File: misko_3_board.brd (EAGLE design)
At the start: 74 x 152 mm, 179 parts, among them IC1 ATMEGA1281-16AU, IC10 ORG1510-MK4, IC11 TPS3808G33DBVT, IC12 LTC4425, IC13 RN-42, IC14 ADXL345, IC15 74HCT1G32, IC16 FM25W256-SOIC, IC17 MICROSD_SPI_MODE, IC18 FH12-30S-0.5SH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

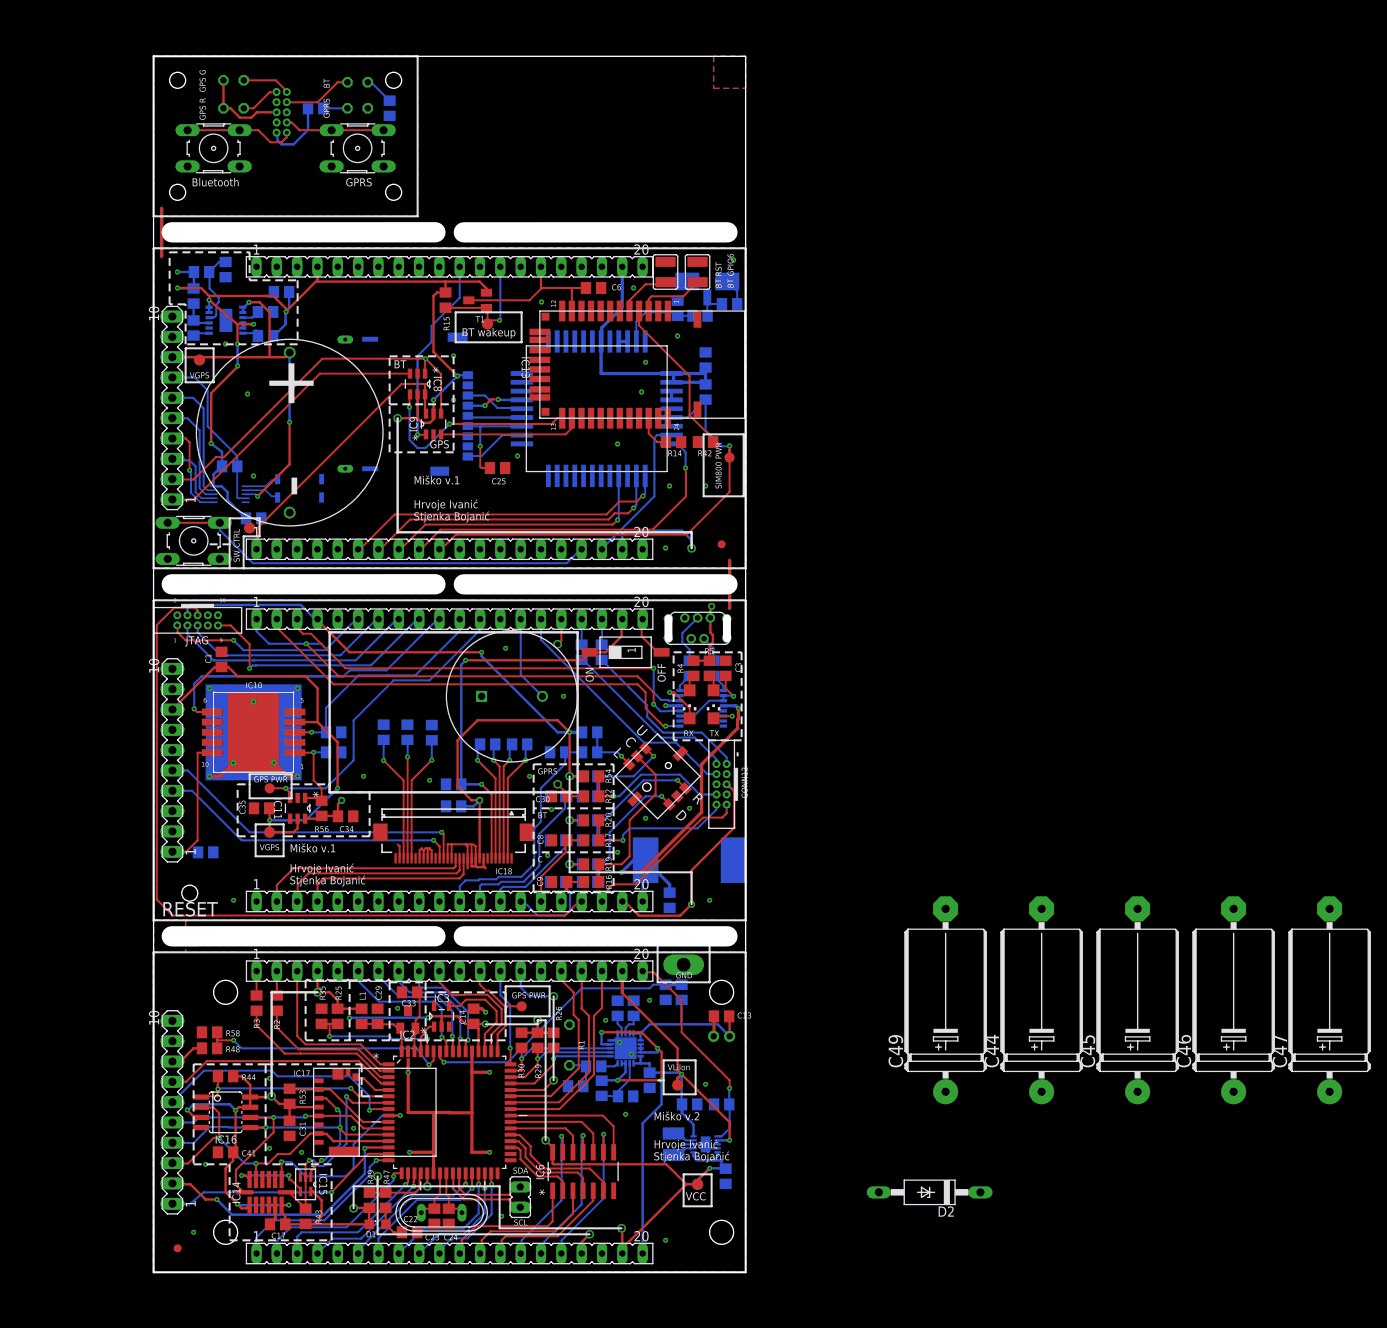
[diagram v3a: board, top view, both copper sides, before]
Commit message: - replaced LTC4425's Vmid capacitor divider by resistors -
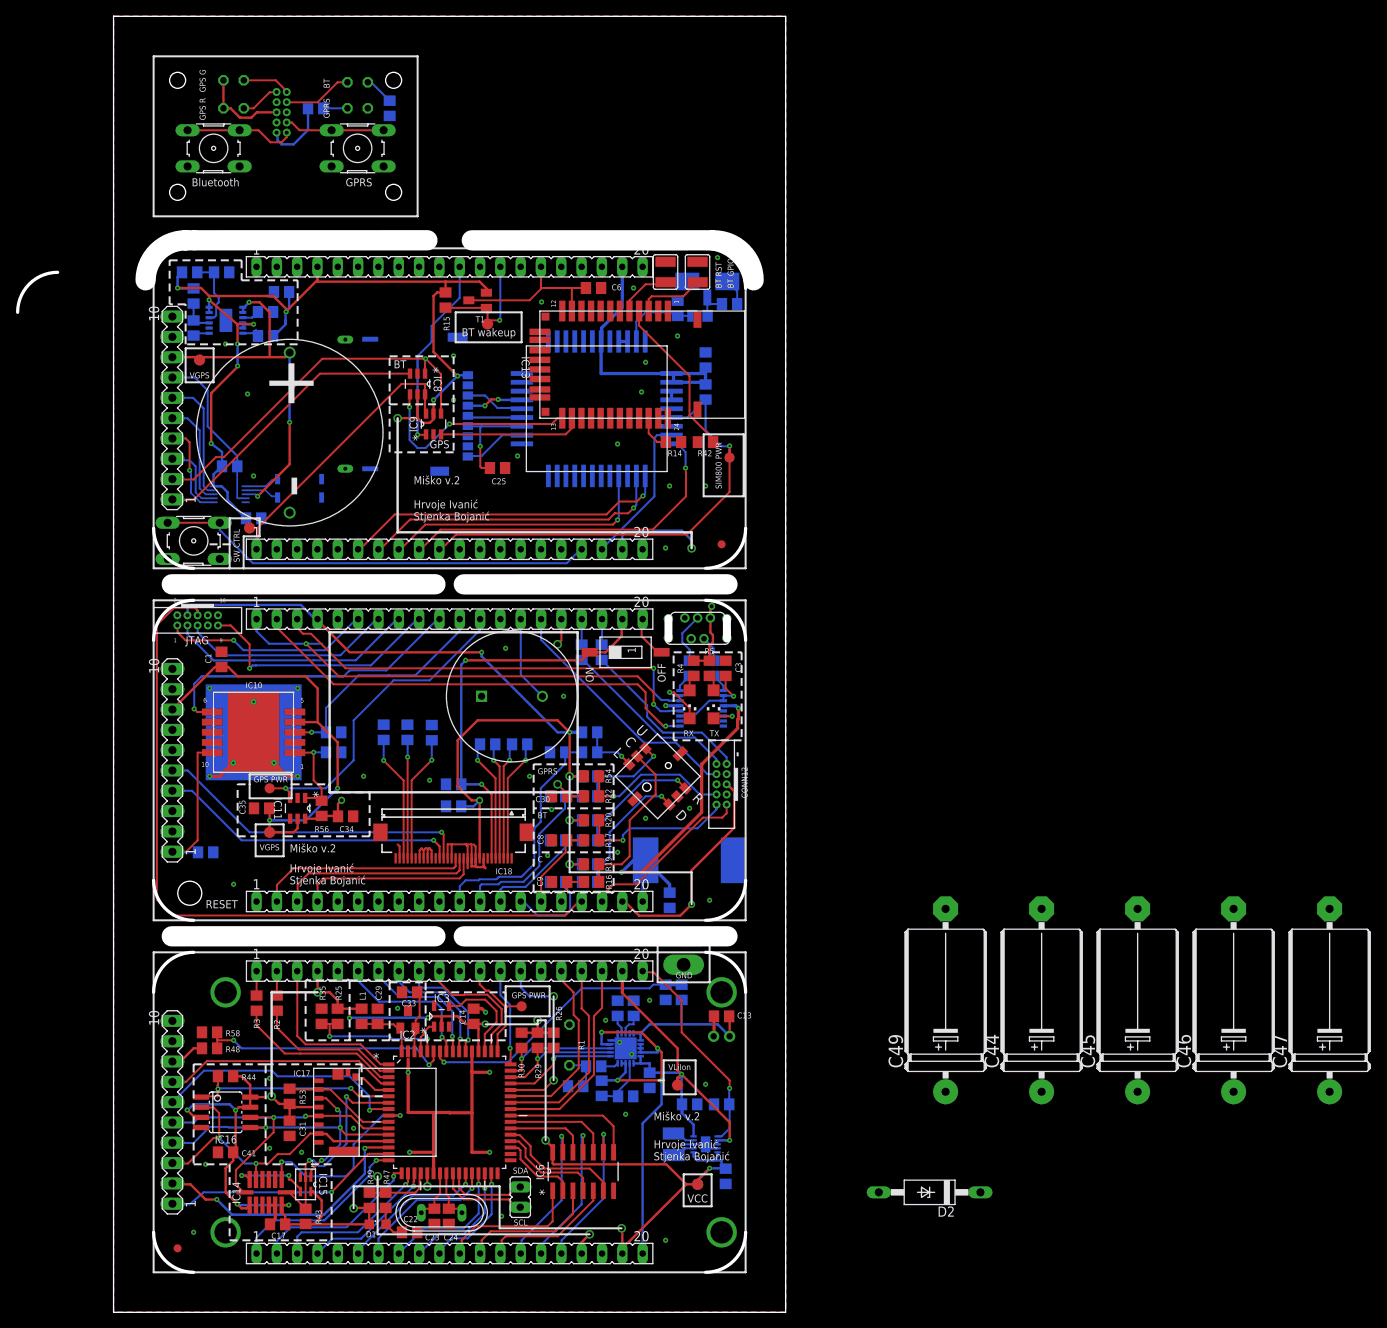
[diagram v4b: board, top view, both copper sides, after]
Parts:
- removed C19, C20: 100µF, rcl:C0805
- added R60, R61: 470k, resistor:R0805
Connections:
- net GND: now also R61.1; no longer C20.1
- net VCC: now also R60.2; no longer C19.1
- net VMID: now also R60.1, R61.2; no longer C19.2, C20.2
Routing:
- net GND: track 121.8 -> 97.8 mm, vias 53 -> 57
- net VCC: track 462.2 -> 459.8 mm, vias 35 -> 34
- net VMID: track 9.76 -> 9.00 mm
- removed copper zone on layer 1, net N$1
- removed copper zone on layer 16, net N$2
- removed copper zone on layer 16, net N$3
- removed copper zone on layer 1, net N$4
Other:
- board size 74 x 152 mm -> 96 x 162 mm
- board text removed: "Miško v.1"

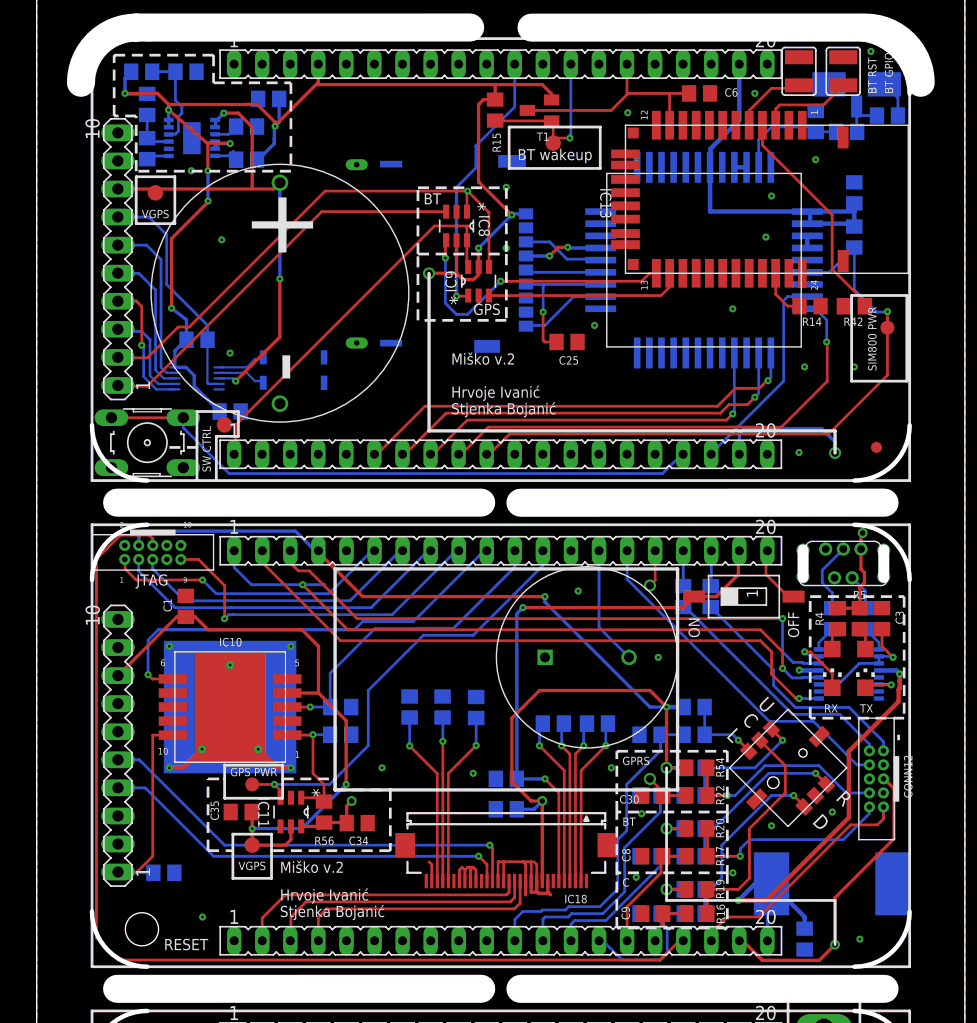
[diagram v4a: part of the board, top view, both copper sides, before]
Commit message: - replaced TH reset switch with smaller SMD part
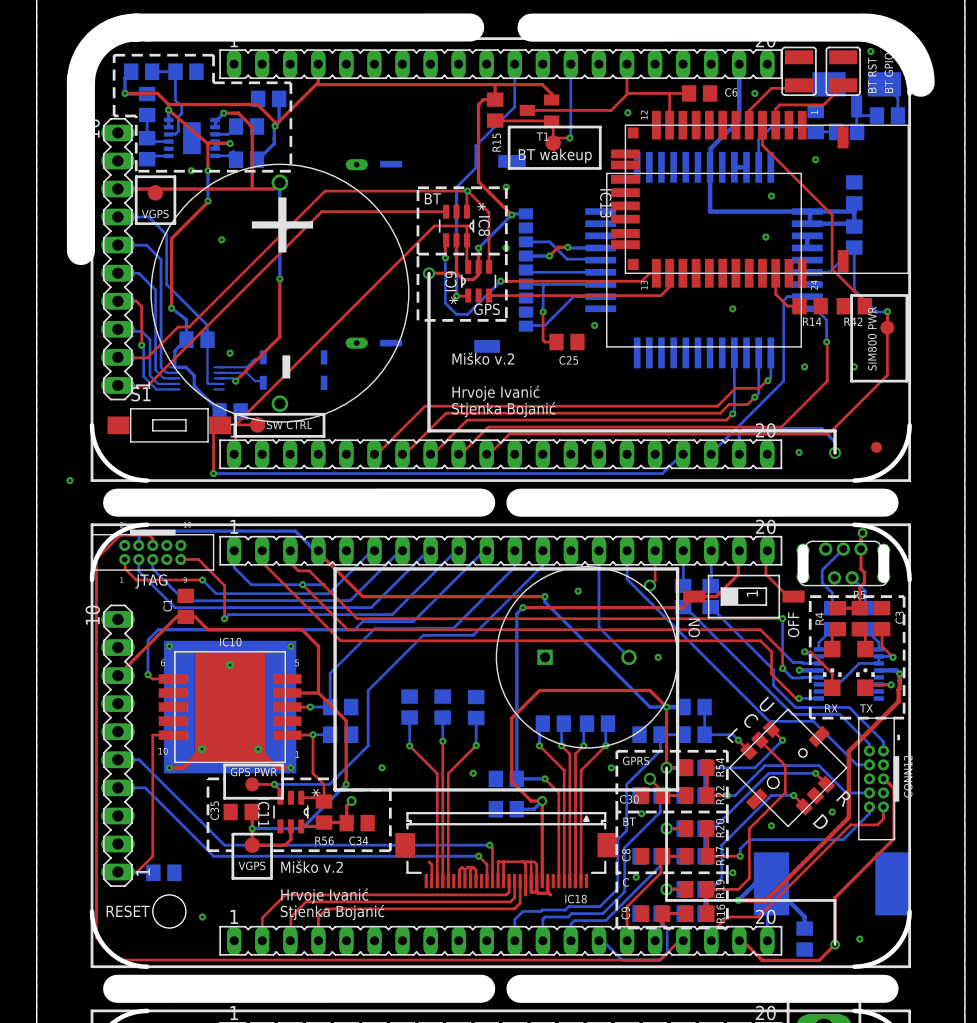
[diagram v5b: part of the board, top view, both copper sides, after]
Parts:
- S1: value RESET -> (none); device switch-omron:B3F-10XX -> DTSM-32N-B:DTSM-32N-B
- moved TP3 3.00 mm to (15.0, 93.0)
- moved S1 2.53 mm to (7.00, 93.0)
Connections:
- net GND: now also S1.1; no longer S1.3, S1.4
- net RESET: no longer S1.1
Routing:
- net RESET: track 164.3 -> 157.0 mm, vias 2 -> 4
- net ANALOG_SW_CTRL_PIN: track 59.1 -> 60.1 mm
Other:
- outline, holes or cut-outs redrawn
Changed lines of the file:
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@@
 <setting verticaltext="up"/>
 </settings>
-<grid distance="0.5" unitdist="mm" unit="mm" style="lines" multiple="1" display="yes" altdistance="0.005" altunitdist="mm" altunit="mm"/>
+<grid distance="1" unitdist="mm" unit="mm" style="lines" multiple="1" display="yes" altdistance="0.005" altunitdist="mm" altunit="mm"/>
 <layers>
 <layer number="1" name="Top" color="4" fill="1" visible="yes" active="yes"/>
@@
 <wire x1="17.99" y1="116.04" x2="17.99" y2="124.04" width="0.25" layer="22" style="shortdash"/>
 <wire x1="5" y1="26" x2="12" y2="26" width="0.254" layer="21" style="shortdash"/>
-<hole x="4.52" y="47.39" drill="3"/>
-<text x="6.5" y="45.5" size="1.016" layer="21">RESET</text>
+<text x="1.2" y="48.5" size="1.016" layer="21">RESET</text>
 <wire x1="22" y1="80" x2="53" y2="80" width="0.3048" layer="21"/>
 <wire x1="53" y1="80" x2="53" y2="60" width="0.3048" layer="21"/>
@@
 <wire x1="7.5" y1="115.5" x2="4" y2="115.5" width="0.25" layer="21"/>
 <wire x1="4" y1="115.5" x2="4" y2="111.25" width="0.25" layer="21"/>
-<text x="10.75" y="88.75" size="0.75" layer="25" rot="R90">SW CTRL</text>
-<wire x1="11.25" y1="92" x2="13.25" y2="92" width="0.25" layer="21"/>
-<wire x1="13.25" y1="92" x2="13.25" y2="94.25" width="0.25" layer="21"/>
-<wire x1="13.25" y1="94.25" x2="9.5" y2="94.25" width="0.25" layer="21"/>
-<wire x1="9.5" y1="94.25" x2="9.5" y2="91" width="0.25" layer="21"/>
-<wire x1="9.5" y1="91" x2="9.5" y2="88" width="0.25" layer="21"/>
-<wire x1="11.25" y1="88" x2="11.25" y2="92" width="0.25" layer="21"/>
+<text x="15.77" y="92.65" size="0.75" layer="25">SW CTRL</text>
 <wire x1="37.75" y1="116.25" x2="46" y2="116.25" width="0.25" layer="21"/>
 <wire x1="46" y1="116.25" x2="46" y2="120" width="0.25" layer="21"/>
@@
 <wire x1="68.75" y1="97" x2="68.75" y2="104.75" width="0.25" layer="21"/>
 <text x="18.5" y="94.75" size="0.75" layer="26">32k768</text>
-<wire x1="7" y1="91" x2="9.5" y2="91" width="0.25" layer="21" style="shortdash"/>
 <wire x1="23.5" y1="93.75" x2="13.25" y2="93.75" width="0.25" layer="22" style="shortdash"/>
 <text x="2.5" y="78.75" size="0.5" layer="21">1</text>
@@
 <wire x1="0" y1="128" x2="74" y2="128" width="0.25" layer="21"/>
 <wire x1="74" y1="128" x2="74" y2="88" width="0.25" layer="21"/>
-<wire x1="74" y1="88" x2="11.25" y2="88" width="0.25" layer="21"/>
-<wire x1="11.25" y1="88" x2="9.5" y2="88" width="0.25" layer="21"/>
-<wire x1="9.5" y1="88" x2="0" y2="88" width="0.25" layer="21"/>
+<wire x1="74" y1="88" x2="0" y2="88" width="0.25" layer="21"/>
 <wire x1="0" y1="88" x2="0" y2="128" width="0.25" layer="21"/>
 <wire x1="0" y1="40" x2="74" y2="40" width="0.25" layer="21"/>
@@
 <dimension x1="-5" y1="-7" x2="79" y2="-7" x3="37" y3="-13" textsize="1.778" layer="48"/>
 <dimension x1="-7" y1="-5" x2="-7" y2="157" x3="-12" y3="76" textsize="1.778" layer="48"/>
+<wire x1="-1" y1="108.77" x2="-1.005" y2="124.225" width="2.54" layer="46"/>
+<wire x1="21" y1="92" x2="21" y2="94" width="0.25" layer="21"/>
+<wire x1="21" y1="94" x2="13" y2="94" width="0.25" layer="21"/>
+<wire x1="13" y1="94" x2="13" y2="92" width="0.25" layer="21"/>
+<wire x1="13" y1="92" x2="21" y2="92" width="0.25" layer="21"/>
+<hole x="7" y="49" drill="3"/>
 </plain>
 <attributes>
@@
 <attribute name="VALUE" x="55.135" y="64.96" size="1.27" layer="28" rot="MR0"/>
 </element>
-<element name="S1" library="switch-omron" package="B3F-10XX" value="RESET" x="5.01" y="91.43" smashed="yes">
-<attribute name="MF" value="" x="5.01" y="91.43" size="1.778" layer="27" display="off"/>
-<attribute name="MPN" value="B3F-1000" x="5.01" y="91.43" size="1.778" layer="27" display="off"/>
-<attribute name="OC_FARNELL" value="176432" x="5.01" y="91.43" size="1.778" layer="27" display="off"/>
-<attribute name="OC_NEWARK" value="36M3542" x="5.01" y="91.43" size="1.778" layer="27" display="off"/>
-<attribute name="VALUE" x="1.962" y="86.35" size="1.27" layer="27" ratio="10"/>
-</element>
 <element name="S2" library="smd-special" package="SMS-001" value="POWER_SWITCH" x="59" y="77.5" smashed="yes" rot="R90">
 <attribute name="VALUE" x="62.175" y="81.056" size="1.27" layer="27" ratio="10" rot="R180"/>
@@
 <attribute name="VALUE" x="13.865" y="59.738" size="0.0254" layer="27"/>
 </element>
-<element name="TP3" library="testpad" package="TP14R" value="Analogue Switch CRTL Pin" x="11.99" y="93.04" smashed="yes">
-<attribute name="TP_SIGNAL_NAME" value="" x="11.99" y="90.5" size="1" layer="37"/>
-<attribute name="VALUE" x="11.482" y="92.278" size="0.0254" layer="27"/>
+<element name="TP3" library="testpad" package="TP14R" value="Analogue Switch CRTL Pin" x="14.99" y="93.04" smashed="yes">
+<attribute name="TP_SIGNAL_NAME" value="" x="14.99" y="90.5" size="1" layer="37"/>
+<attribute name="VALUE" x="14.482" y="92.278" size="0.0254" layer="27"/>
 </element>
 <element name="TP8" library="testpad" package="TP14R" value="VLiIon Regulated" x="65.5" y="23.4" smashed="yes">
@@
 <element name="R60" library="resistor" package="R0805" value="470k" x="4.5" y="125" rot="MR0"/>
 <element name="R61" library="resistor" package="R0805" value="470k" x="8.5" y="125" rot="MR0"/>
+<element name="S1" library="DTSM-32N-B" package="DTSM-32N-B" value="" x="7" y="93">
+<attribute name="MF" value="" x="7" y="93" size="1.778" layer="27" display="off"/>
+<attribute name="MPN" value="B3F-1000" x="7" y="93" size="1.778" layer="27" display="off"/>
+<attribute name="OC_FARNELL" value="176432" x="7" y="93" size="1.778" layer="27" display="off"/>
+<attribute name="OC_NEWARK" value="36M3542" x="7" y="93" size="1.778" layer="27" display="off"/>
+</element>
 </elements>
 <signals>
@@
 <wire x1="33.99" y1="111.04" x2="30.99" y2="111.04" width="0.254" layer="1"/>
 <contactref element="TP3" pad="TP"/>
-<wire x1="11.99" y1="93.04" x2="12.99" y2="93.04" width="0.254" layer="1"/>
+<wire x1="14.99" y1="93.04" x2="12.99" y2="93.04" width="0.254" layer="1"/>
 <wire x1="15" y1="6.5" x2="21.33551875" y2="6.5" width="0.25" layer="16"/>
 <wire x1="21.33551875" y1="6.5" x2="27.005009375" y2="12.169490625" width="0.25" layer="16"/>
@@
 <signal name="RESET" class="3">
 <contactref element="IC1" pad="20"/>
-<contactref element="S1" pad="1"/>
-<contactref element="S1" pad="2"/>
 <contactref element="R47" pad="2"/>
 <contactref element="R49" pad="2"/>
@@
 <contactref element="CONN9" pad="17"/>
 <via x="54.5" y="4.75" extent="1-16" drill="0.7" shape="octagon"/>
-<wire x1="1.7588" y1="93.6906" x2="8.2612" y2="93.6906" width="0.25" layer="1"/>
 <wire x1="32.3" y1="9.95" x2="32.683275" y2="9.95" width="0.25" layer="1"/>
 <wire x1="32.683275" y1="9.95" x2="32.781275" y2="10.048" width="0.25" layer="1"/>
@@
 <wire x1="53.1653875" y1="46.35" x2="51.4195875" y2="44.6042" width="0.25" layer="1"/>
 <wire x1="51.4195875" y1="44.6042" x2="2.3958" y2="44.6042" width="0.25" layer="1"/>
-<wire x1="12.4104125" y1="88.6342" x2="51.6342" y2="88.6342" width="0.25" layer="16"/>
-<wire x1="53.5" y1="90.5" x2="51.6342" y2="88.6342" width="0.25" layer="16"/>
-<wire x1="8.2612" y1="93.6906" x2="8.2612" y2="92.7834125" width="0.25" layer="16"/>
-<wire x1="8.2612" y1="92.7834125" x2="12.4104125" y2="88.6342" width="0.25" layer="16"/>
+<wire x1="51.6342" y1="88.6342" x2="53.5" y2="90.5" width="0.25" layer="16"/>
 <wire x1="53.5" y1="90.38" x2="53.5" y2="90.5" width="0.25" layer="16"/>
 <contactref element="CONN10" pad="6"/>
@@
 <wire x1="2.57519375" y1="83.059" x2="5.191" y2="83.059" width="0.25" layer="1"/>
 <wire x1="5.191" y1="83.059" x2="5.5" y2="82.75" width="0.25" layer="1"/>
-<wire x1="5.5" y1="82.75" x2="12.4104125" y2="88.6342" width="0" layer="19" extent="1-16"/>
+<via x="-2" y="88" extent="1-16" drill="0.25"/>
+<contactref element="S1" pad="2"/>
+<wire x1="11" y1="88.6342" x2="51.6342" y2="88.6342" width="0.25" layer="16"/>
+<wire x1="11.6" y1="93" x2="11" y2="92.4" width="0.25" layer="1"/>
+<wire x1="11" y1="92.4" x2="11" y2="88.6342" width="0.25" layer="1"/>
+<via x="11" y="88.6342" extent="1-16" drill="0.25"/>
+<wire x1="5.5" y1="82.75" x2="11" y2="88.6342" width="0" layer="19" extent="1-16"/>
+<wire x1="-2" y1="88" x2="2.509" y2="83.009" width="0" layer="19" extent="1-1"/>
 <wire x1="33.3932" y1="12.38" x2="51.4195875" y2="44.6042" width="0" layer="19" extent="1-1"/>
 <wire x1="28" y1="9.95" x2="29" y2="9.95" width="0" layer="19" extent="1-1"/>
@@
 <contactref element="C23" pad="1"/>
 <contactref element="C24" pad="1"/>
-<contactref element="S1" pad="3"/>
-<contactref element="S1" pad="4"/>
 <contactref element="C22" pad="1"/>
 <contactref element="IC2" pad="3"/>
@@
 <via x="9" y="35" extent="1-16" drill="2.8"/>
 <contactref element="R61" pad="1"/>
+<contactref element="S1" pad="1"/>
 <wire x1="135" y1="45.43" x2="147" y2="45.43" width="0" layer="19" extent="1-1"/>
 <wire x1="123" y1="45.43" x2="135" y2="45.43" width="0" layer="19" extent="1-1"/>
@@
 <wire x1="99" y1="45.43" x2="111" y2="45.43" width="0" layer="19" extent="1-1"/>
 <wire x1="69.5" y1="46.5" x2="99" y2="45.43" width="0" layer="19" extent="1-1"/>
+<wire x1="49.8" y1="48.8" x2="49.55" y2="48.8" width="0" layer="19" extent="1-16"/>
 <wire x1="49.55" y1="59.5" x2="49.8" y2="59.5" width="0" layer="19" extent="1-16"/>
 <wire x1="59" y1="28" x2="59.75" y2="27.25" width="0" layer="19" extent="16-16"/>
-<wire x1="49.55" y1="48.8" x2="49.25" y2="52.1" width="0" layer="19" extent="16-16"/>
-<wire x1="49.8" y1="48.8" x2="49.55" y2="48.8" width="0" layer="19" extent="1-16"/>
 </signal>
 <signal name="GPRS_LED" class="2">
